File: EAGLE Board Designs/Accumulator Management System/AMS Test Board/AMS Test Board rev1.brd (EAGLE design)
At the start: 386.6 x 87.7 mm, 104 parts, among them J1 CONNECTOR-2__B2B-PH-K, J10 CONNECTOR-2__B2B-PH-K, J11 CONNECTOR-2__B2B-PH-K, J12 CONNECTOR-2__B2B-PH-K, J13 CONNECTOR-2__B2B-PH-K, J14 CONNECTOR-2__B2B-PH-K, J15 CONNECTOR-2__B2B-PH-K, J16 CONNECTOR-2__B2B-PH-K, J17 CONNECTOR-2__B2B-PH-K, J18 CONNECTOR-2__B2B-PH-K, J19 CONNECTOR-2__B2B-PH-K, J2 CONNECTOR-2__B2B-PH-K, J20 CONNECTOR-2__B2B-PH-K, J21 CONNECTOR-2__B2B-PH-K, J22 CONNECTOR-1_5222, J23 CONNECTOR-1_5222, J24 CONNECTOR-1_5222, J25 CONNECTOR-1_5222, J26 CONNECTOR-1_5222, J27 CONNECTOR-1_5222, J28 CONNECTOR-1_5222, J29 CONNECTOR-1_5222, J3 CONNECTOR-2__B2B-PH-K, J30 CONNECTOR-1_5222, J31 CONNECTOR-1_5222, J32 CONNECTOR-1_5222, J33 CONNECTOR-1_5222, J34 CONNECTOR-1_5222, J35 CONNECTOR-1_5222, J36 CONNECTOR-1_5222, J37 CONNECTOR-1_5222, J38 CONNECTOR-1_5222, J39 CONNECTOR-1_5222, J4 CONNECTOR-2__B2B-PH-K, J40 CONNECTOR-1_5222, J41 CONNECTOR-1_5222, J42 CONNECTOR-1_5222, J43 CONNECTOR-1_5222, J44 CONNECTOR-2_MF_T_V_, J5 CONNECTOR-2__B2B-PH-K, J6 CONNECTOR-2__B2B-PH-K, J7 CONNECTOR-2__B2B-PH-K, J8 CONNECTOR-2__B2B-PH-K, J9 CONNECTOR-2__B2B-PH-K, T1 TRANSFORMER_HM2112ZNLT_AIRGAP, U1 LTC6820

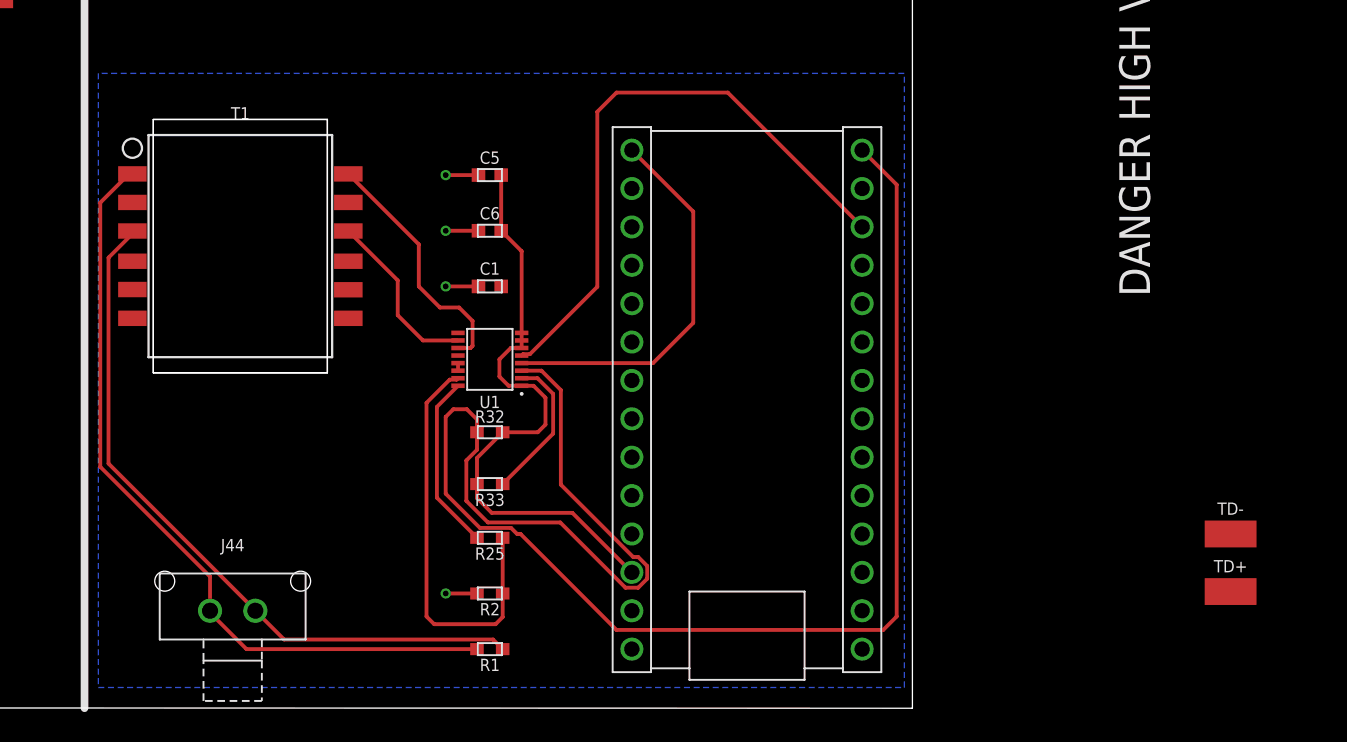
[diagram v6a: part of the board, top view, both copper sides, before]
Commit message: Update AMS Test Board rev1.brd
Drafted a routing for the right side of the board. There's still two wires that are too close to each other.
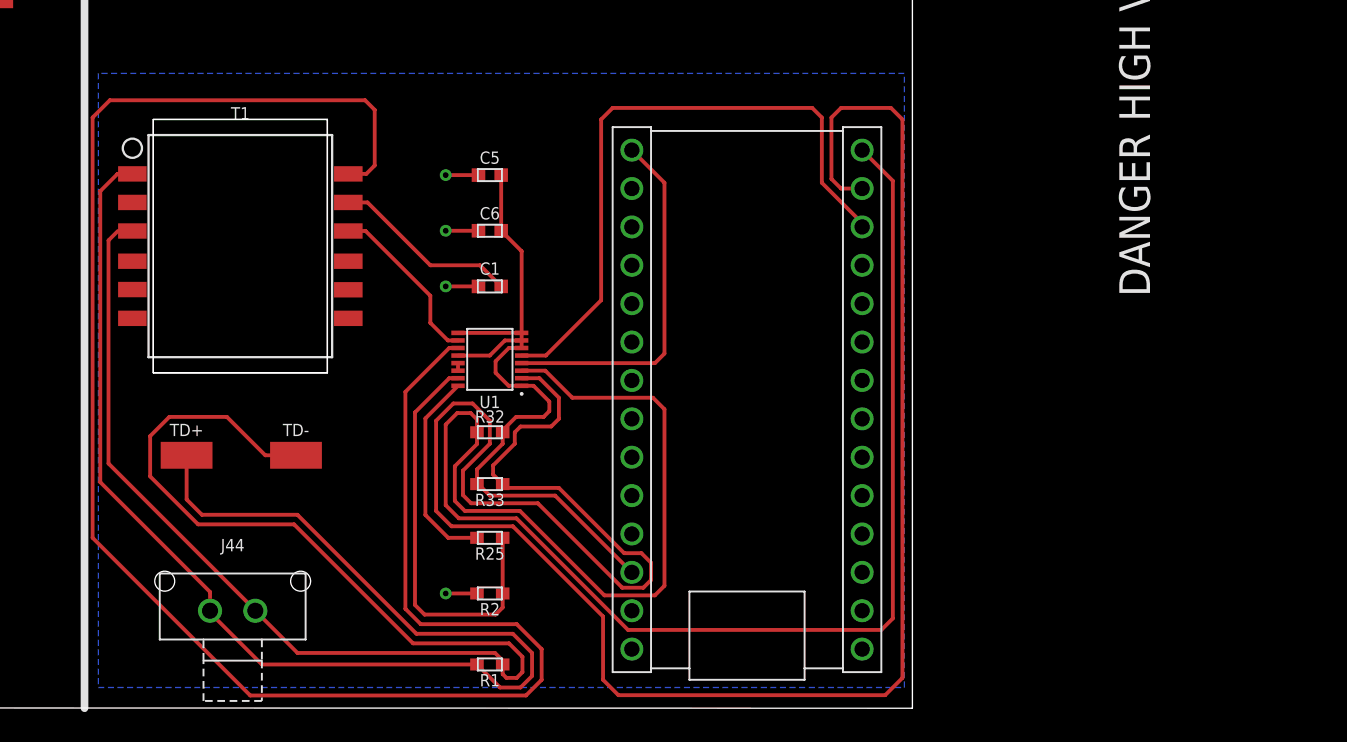
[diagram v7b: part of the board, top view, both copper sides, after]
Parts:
- moved TD+ 69.7 mm to (338.6, 16.6)
- moved TD- 62.1 mm to (345.8, 16.6)
- moved R1 1.02 mm to (358.6, 2.79)
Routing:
- net N$26: track 9.87 -> 143.8 mm
- net IP: track 16.6 -> 118.5 mm
- net TD-: track 48.0 -> 94.1 mm
- net TD+: track 52.3 -> 88.7 mm
- net N$23: track 0.00 -> 12.4 mm
- net +3V3: track 40.7 -> 49.2 mm
- net N$25: track 111.8 -> 118.0 mm
- net N$27: track 40.2 -> 42.3 mm
- net N$30: track 11.7 -> 13.5 mm
- net N$24: track 25.6 -> 24.1 mm
